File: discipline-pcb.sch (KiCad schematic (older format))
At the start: 164 parts, among them J1 AVR-ISP-6, SW1 KEYSW, SW10 KEYSW, SW11 KEYSW, SW12 KEYSW, SW13 KEYSW, SW14 KEYSW, SW15 KEYSW, SW16 KEYSW, SW17 KEYSW, SW18 KEYSW, SW19 KEYSW, SW2 KEYSW, SW20 KEYSW, SW21 KEYSW, SW22 KEYSW, SW23 KEYSW, SW24 KEYSW, SW25 KEYSW, SW26 KEYSW, SW27 KEYSW, SW28 KEYSW, SW29 KEYSW, SW3 KEYSW, SW30 KEYSW, SW31 KEYSW, SW32 KEYSW, SW33 KEYSW, SW34 KEYSW, SW35 KEYSW, SW36 KEYSW, SW37 KEYSW, SW38 KEYSW, SW39 KEYSW, SW4 KEYSW, SW40 KEYSW, SW41 KEYSW, SW42 KEYSW, SW43 KEYSW, SW44 KEYSW, SW45 KEYSW, SW46 KEYSW, SW47 KEYSW, SW48 KEYSW, SW49 KEYSW, SW5 KEYSW, SW50 KEYSW, SW51 KEYSW, SW52 KEYSW, SW53 KEYSW, SW54 KEYSW, SW55 KEYSW, SW56 KEYSW, SW57 KEYSW, SW58 KEYSW, SW59 KEYSW, SW6 KEYSW, SW60 KEYSW, SW61 KEYSW, SW62 KEYSW, SW63 KEYSW, SW64 KEYSW, SW65 KEYSW, SW66 KEYSW, SW67 KEYSW, SW68 KEYSW, SW69 KEYSW, SW7 KEYSW, SW70 KEYSW, SW71 KEYSW, SW72 KEYSW, SW73 KEYSW, SW74 KEYSW, SW8 KEYSW, SW9 KEYSW, U1 ATmega32A-PU, Y1 Crystal

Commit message: Learning stuff
WIP for an attempt to create an ISO layout + split spacebar + middle
button
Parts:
- removed SW70, SW71, SW73, SW74: KEYSW, cftkb:SW_Cherry_MX1A_1.50u_PCBNOSCREEN, symbol keyboard_parts:KEYSW
- removed SW72: KEYSW, cftkb:SW_Cherry_MX1A_1.00u_PCB-NOSCREEN, symbol keyboard_parts:KEYSW
- added D71, D72: (no value), cftkb:D_DO-35_SOD27_P5.08mm_Horizontal, symbol discipline-pcb-rescue:D-Device
- added SW71: KEYSW, cftkb:SW_Cherry_MX1A_1.00u_PCB-NOSCREEN, symbol discipline-pcb-rescue:KEYSW-keyboard_parts
- added SW72, SW73: KEYSW, cftkb:SW_Cherry_MX1A_3.00u_PCB-NOSCREEN, symbol discipline-pcb-rescue:KEYSW-keyboard_parts
- BOOT1, RESET1: symbol keyboard_parts:SW_PUSH -> discipline-pcb-rescue:SW_PUSH-keyboard_parts
- C1, C2, C4, C5: symbol Device:C_Small -> discipline-pcb-rescue:C_Small-Device
- C3: symbol Device:CP1_Small -> discipline-pcb-rescue:CP1_Small-Device
- D1, D10, D11, D12, D13, D14, D15, D16, D17, D18, D19, D2, D20, D21, D22, D23, D24, D25, D26, D27, D28, D29, D3, D30, D31, D32, D33, D34, D35, D36, D37, D38, D39, D4, D40, D41, D42, D43, D44, D45, D46, D47, D48, D49, D5, D50, D51, D52, D53, D54, D55, D56, D57, D58, D59, D6, D60, D61, D62, D63, D64, D65, D66, D67, D68, D7, D8, D9: symbol Device:D -> discipline-pcb-rescue:D-Device
- D69, D70: symbol Device:D_Zener_Small -> discipline-pcb-rescue:D_Zener_Small-Device
- F1: symbol Device:Polyfuse_Small -> discipline-pcb-rescue:Polyfuse_Small-Device
- J1: symbol Connector:AVR-ISP-6 -> discipline-pcb-rescue:AVR-ISP-6-Connector
- LED1: symbol Device:LED -> discipline-pcb-rescue:LED-Device
- R1, R2, R3, R4, R5, R6, R7: symbol Device:R_Small -> discipline-pcb-rescue:R_Small-Device
- SW1, SW10, SW11, SW12, SW13, SW14, SW15, SW16, SW17, SW18, SW19, SW2, SW20, SW21, SW22, SW23, SW24, SW25, SW26, SW27, SW28, SW29, SW3, SW30, SW31, SW32, SW33, SW34, SW35, SW36, SW37, SW38, SW39, SW4, SW40, SW41, SW42, SW44, SW46, SW47, SW48, SW49, SW5, SW50, SW51, SW52, SW53, SW54, SW55, SW56, SW57, SW58, SW6, SW62, SW65, SW66, SW67, SW68, SW69, SW7, SW8, SW9: symbol keyboard_parts:KEYSW -> discipline-pcb-rescue:KEYSW-keyboard_parts
- SW43: footprint cftkb:SW_Cherry_MX1A_2.25u_PCBNOSCREEN -> cftkb:SW_Cherry_MX1A_1.00u_PCB-NOSCREEN; symbol keyboard_parts:KEYSW -> discipline-pcb-rescue:KEYSW-keyboard_parts
- SW45: footprint cftkb:SW_Cherry_MX1A_2.25u_PCBNOSCREEN -> cftkb:SW_Cherry_MX1A_1.25u_PCBNOSCREEN; symbol keyboard_parts:KEYSW -> discipline-pcb-rescue:KEYSW-keyboard_parts
- SW59, SW60, SW61, SW63, SW64: footprint cftkb:SW_Cherry_MX1A_1.25u_PCBNOSCREEN -> cftkb:SW_Cherry_MX1A_1.00u_PCB-NOSCREEN; symbol keyboard_parts:KEYSW -> discipline-pcb-rescue:KEYSW-keyboard_parts
- U1: symbol MCU_Microchip_ATmega:ATmega32A-PU -> discipline-pcb-rescue:ATmega32A-PU-MCU_Microchip_ATmega
- USB1: symbol Type-C:USB_C_GCT_USB4085 -> discipline-pcb-rescue:USB_C_GCT_USB4085-Type-C
- Y1: symbol Device:Crystal -> discipline-pcb-rescue:Crystal-Device
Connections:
- wire segments 342 -> 340

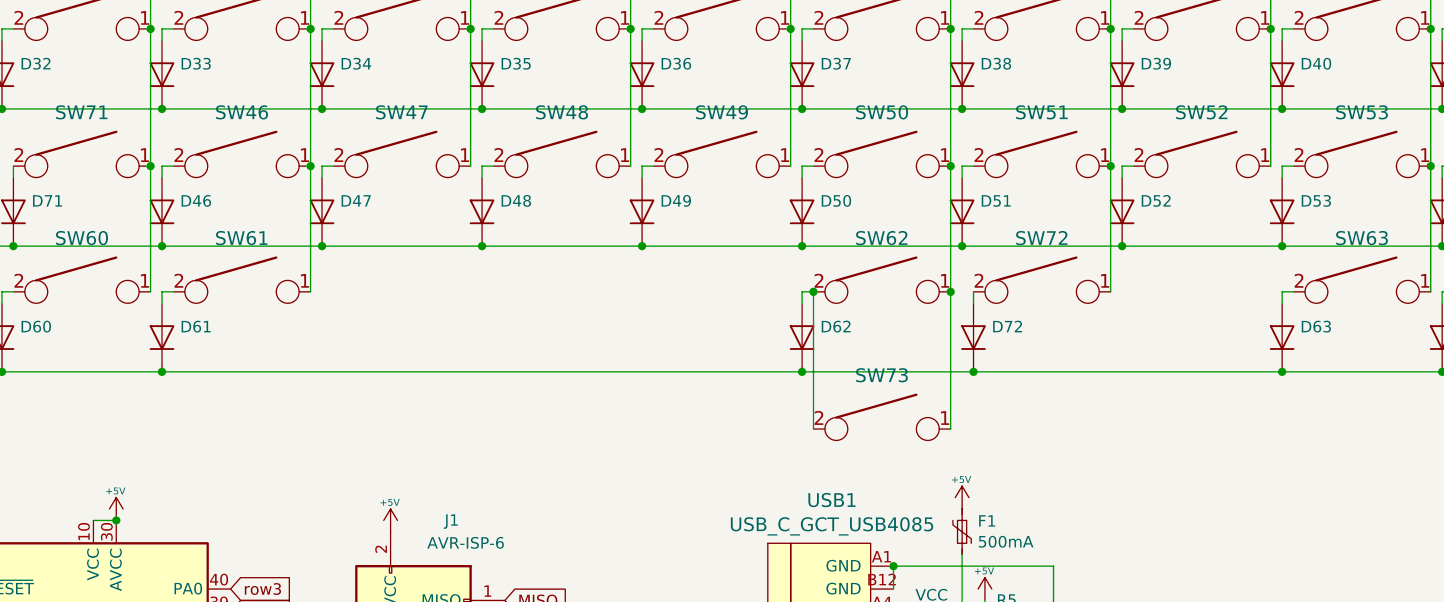
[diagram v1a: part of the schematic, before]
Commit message: Learning stuff
WIP for an attempt to create an ISO layout + split spacebar + middle
button
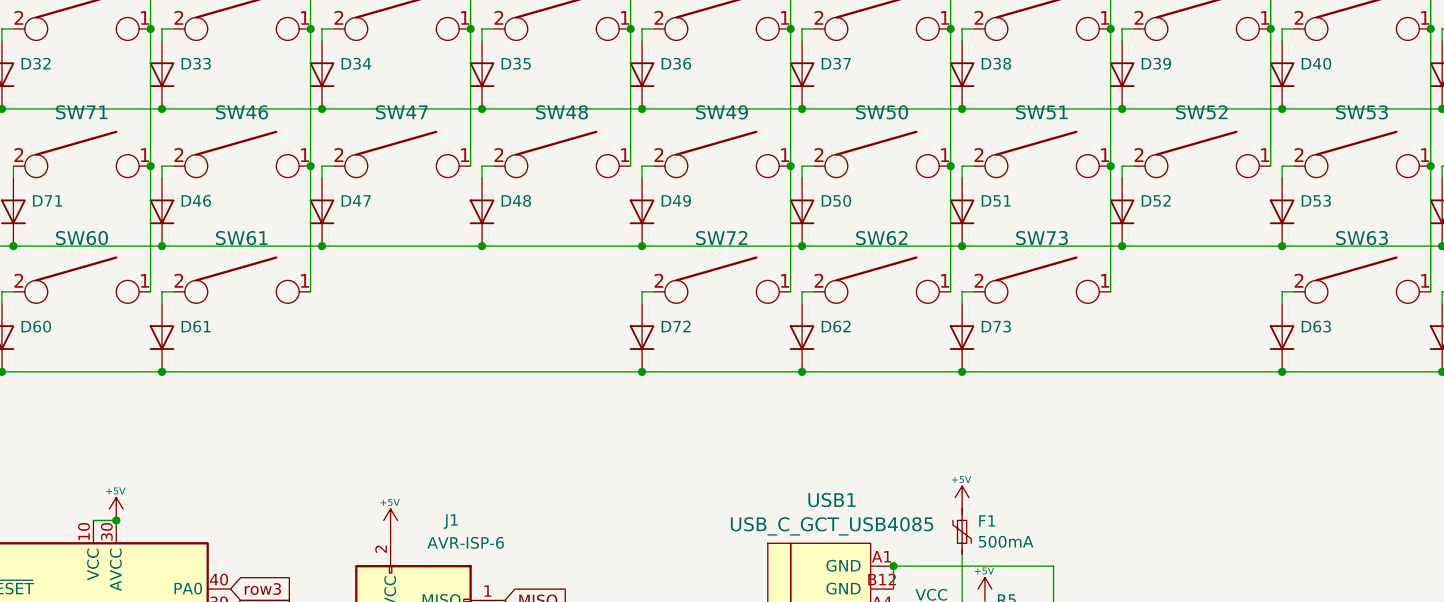
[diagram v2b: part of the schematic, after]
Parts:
- added D73: (no value), cftkb:D_DO-35_SOD27_P5.08mm_Horizontal, symbol discipline-pcb-rescue:D-Device
- C1, C2: footprint cftkb:D_DO-35_SOD27_P5.08mm_Horizontal -> cftkb:C_Disc_D3.0mm_W1.6mm_P2.50mm
- C3: footprint cftkb:D_DO-35_SOD27_P5.08mm_Horizontal -> cftkb:CP_Radial_D4.0mm_P1.50mm
- C4, C5: footprint cftkb:D_DO-35_SOD27_P5.08mm_Horizontal -> cftkb:C_Disc_D4.3mm_W1.9mm_P5.00mm
- SW29: footprint cftkb:SW_Cherry_MX1A_1.50u_PCBNOSCREEN -> cftkb:SW_Cherry_MX1A_ISOEnter_PCB_ReversedStabilizer
- SW72, SW73: footprint cftkb:SW_Cherry_MX1A_3.00u_PCB-NOSCREEN -> cftkb:SW_Cherry_MX1A_3.00u_PCBNOSCREEN
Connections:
- net col5: now also SW72.1
- net col6: no longer SW73.1
- net col7: now also SW73.1; no longer SW72.1
- net row4: now also D73.1 (K)
- net at D62.2 (A), SW62.2: no longer SW73.2
- new net: D73.2 (A), SW73.2
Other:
- moved on the sheet: D72, SW72, SW73
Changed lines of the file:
@@
 F 0 "SW29" H 12350 3733 60  0000 C CNN
 F 1 "KEYSW" H 12350 3400 60  0001 C CNN
-F 2 "cftkb:SW_Cherry_MX1A_1.50u_PCBNOSCREEN" H 12350 3500 60  0001 C CNN
+F 2 "cftkb:SW_Cherry_MX1A_ISOEnter_PCB_ReversedStabilizer" H 12350 3500 60  0001 C CNN
 F 3 "" H 12350 3500 60  0000 C CNN
 	1    12350 3500
@@
 	3600 5600 4300 5600
 Connection ~ 4300 5600
-Wire Wire Line
-	4300 5600 7100 5600
 Wire Wire Line
 	11300 5600 12000 5600
@@
 Wire Wire Line
 	10600 5250 10600 5300
-Connection ~ 7100 5600
 Wire Wire Line
 	9200 5600 9900 5600
@@
 F 0 "C2" H 3100 7300 50  0000 L CNN
 F 1 "22p" H 3100 7200 50  0000 L CNN
-F 2 "cftkb:D_DO-35_SOD27_P5.08mm_Horizontal" H 3000 7200 50  0001 C CNN
+F 2 "cftkb:C_Disc_D3.0mm_W1.6mm_P2.50mm" H 3000 7200 50  0001 C CNN
 F 3 "~" H 3000 7200 50  0001 C CNN
 	1    3000 7200
@@
 F 0 "C1" H 2650 7300 50  0000 L CNN
 F 1 "22p" H 2600 7200 50  0000 L CNN
-F 2 "cftkb:D_DO-35_SOD27_P5.08mm_Horizontal" H 2850 7200 50  0001 C CNN
+F 2 "cftkb:C_Disc_D3.0mm_W1.6mm_P2.50mm" H 2850 7200 50  0001 C CNN
 F 3 "~" H 2850 7200 50  0001 C CNN
 	1    2850 7200
@@
 F 0 "C3" H 5350 10250 50  0000 L CNN
 F 1 "4.7u" H 5300 9950 50  0000 L CNN
-F 2 "cftkb:D_DO-35_SOD27_P5.08mm_Horizontal" H 5400 10100 50  0001 C CNN
+F 2 "cftkb:CP_Radial_D4.0mm_P1.50mm" H 5400 10100 50  0001 C CNN
 F 3 "~" H 5400 10100 50  0001 C CNN
 	1    5400 10100
@@
 F 0 "C4" H 5500 10250 50  0000 L CNN
 F 1 "0.1u" H 5500 9950 50  0000 L CNN
-F 2 "cftkb:D_DO-35_SOD27_P5.08mm_Horizontal" H 5550 10100 50  0001 C CNN
+F 2 "cftkb:C_Disc_D4.3mm_W1.9mm_P5.00mm" H 5550 10100 50  0001 C CNN
 F 3 "~" H 5550 10100 50  0001 C CNN
 	1    5550 10100
@@
 F 0 "C5" H 5650 10250 50  0000 L CNN
 F 1 "0.1u" H 5700 9950 50  0000 L CNN
-F 2 "cftkb:D_DO-35_SOD27_P5.08mm_Horizontal" H 5700 10100 50  0001 C CNN
+F 2 "cftkb:C_Disc_D4.3mm_W1.9mm_P5.00mm" H 5700 10100 50  0001 C CNN
 F 3 "~" H 5700 10100 50  0001 C CNN
 	1    5700 10100
@@
 Wire Wire Line
 	7750 4100 7750 4700
-Connection ~ 7750 4700
-Wire Wire Line
-	7750 4700 7750 5250
 Wire Wire Line
 	8450 2900 8450 2950
@@
 	8450 3500 8450 4100
 Connection ~ 8450 4100
-Wire Wire Line
-	8450 4100 8450 4700
 Wire Wire Line
 	9150 2900 9150 2950
@@
 	1    0    0    -1
 $EndComp
-Connection ~ 8450 4700
-Wire Wire Line
-	8450 4700 8450 5250
+Wire Wire Line
+	7750 4700 7750 5250
 $Comp
 L discipline-pcb-rescue:KEYSW-keyboard_parts SW72
 U 1 1 5EFCCC86
-P 8150 5250
-F 0 "SW72" H 8150 5483 60  0000 C CNN
-F 1 "KEYSW" H 8150 5150 60  0001 C CNN
-F 2 "cftkb:SW_Cherry_MX1A_3.00u_PCB-NOSCREEN" H 8150 5250 60  0001 C CNN
-F 3 "" H 8150 5250 60  0000 C CNN
-	1    8150 5250
+P 6750 5250
+F 0 "SW72" H 6750 5483 60  0000 C CNN
+F 1 "KEYSW" H 6750 5150 60  0001 C CNN
+F 2 "cftkb:SW_Cherry_MX1A_3.00u_PCBNOSCREEN" H 6750 5250 60  0001 C CNN
+F 3 "" H 6750 5250 60  0000 C CNN
+	1    6750 5250
 	1    0    0    -1
 $EndComp
@@
 L discipline-pcb-rescue:D-Device D72
 U 1 1 5EFEEE87
-P 7850 5450
-F 0 "D72" V 7896 5371 50  0000 R CNN
-F 1 " " V 7805 5371 50  0000 R CNN
-F 2 "cftkb:D_DO-35_SOD27_P5.08mm_Horizontal" H 7850 5450 50  0001 C CNN
-F 3 "~" H 7850 5450 50  0001 C CNN
-	1    7850 5450
-	0    -1   -1   0
-$EndComp
-Connection ~ 7850 5600
-Wire Wire Line
-	7850 5600 9200 5600
-Wire Wire Line
-	7850 5250 7850 5300
+P 6400 5450
+F 0 "D72" V 6446 5371 50  0000 R CNN
+F 1 " " V 6355 5371 50  0000 R CNN
+F 2 "cftkb:D_DO-35_SOD27_P5.08mm_Horizontal" H 6400 5450 50  0001 C CNN
+F 3 "~" H 6400 5450 50  0001 C CNN
+	1    6400 5450
+	0    -1   -1   0
+$EndComp
+Wire Wire Line
+	6400 5250 6400 5300
 $Comp
 L discipline-pcb-rescue:KEYSW-keyboard_parts SW71
@@
 L discipline-pcb-rescue:KEYSW-keyboard_parts SW73
 U 1 1 5EFB299D
-P 7450 5850
-F 0 "SW73" H 7450 6083 60  0000 C CNN
-F 1 "KEYSW" H 7450 5750 60  0001 C CNN
-F 2 "cftkb:SW_Cherry_MX1A_3.00u_PCB-NOSCREEN" H 7450 5850 60  0001 C CNN
-F 3 "" H 7450 5850 60  0000 C CNN
-	1    7450 5850
-	1    0    0    -1
-$EndComp
-Wire Wire Line
-	7750 5850 7750 5250
-Connection ~ 7750 5250
-Wire Wire Line
-	7100 5600 7850 5600
-Wire Wire Line
-	7150 5850 7150 5250
-Connection ~ 7150 5250
+P 8150 5250
+F 0 "SW73" H 8150 5483 60  0000 C CNN
+F 1 "KEYSW" H 8150 5150 60  0001 C CNN
+F 2 "cftkb:SW_Cherry_MX1A_3.00u_PCBNOSCREEN" H 8150 5250 60  0001 C CNN
+F 3 "" H 8150 5250 60  0000 C CNN
+	1    8150 5250
+	1    0    0    -1
+$EndComp
+Connection ~ 7750 4700
+Wire Wire Line
+	8450 4100 8450 4700
+Wire Wire Line
+	8450 4700 8450 5250
+Connection ~ 8450 4700
+Wire Wire Line
+	4300 5600 6400 5600
+Connection ~ 7100 5600
+Wire Wire Line
+	7100 5600 7800 5600
+Connection ~ 6400 5600
+Wire Wire Line
+	6400 5600 7100 5600
+$Comp
+L discipline-pcb-rescue:D-Device D73
+U 1 1 5F273FC2
+P 7800 5450
+F 0 "D73" V 7846 5371 50  0000 R CNN
+F 1 " " V 7755 5371 50  0000 R CNN
+F 2 "cftkb:D_DO-35_SOD27_P5.08mm_Horizontal" H 7800 5450 50  0001 C CNN
+F 3 "~" H 7800 5450 50  0001 C CNN
+	1    7800 5450
+	0    -1   -1   0
+$EndComp
+Wire Wire Line
+	6450 5250 6400 5250
+Connection ~ 7800 5600
+Wire Wire Line
+	7800 5600 9200 5600
+Wire Wire Line
+	7850 5250 7800 5250
+Wire Wire Line
+	7800 5250 7800 5300
+Wire Wire Line
+	7050 4700 7050 5250
+Connection ~ 7050 4700
 $EndSCHEMATC

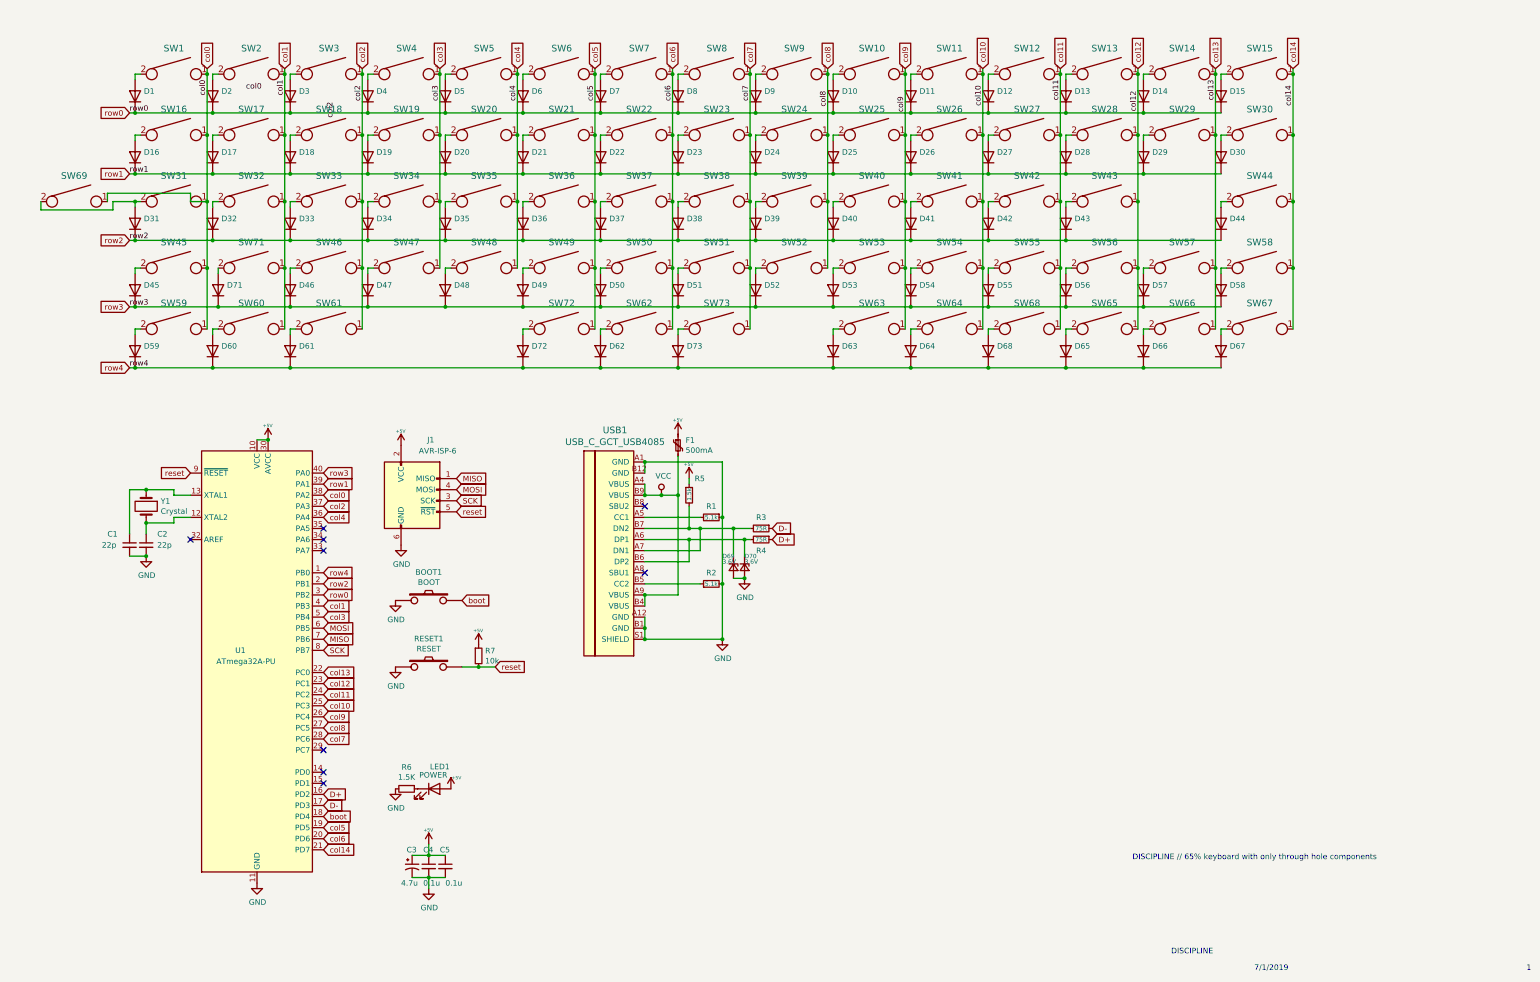
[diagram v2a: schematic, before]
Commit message: "Split spacebar + middle button" design completed
Re-integrated ANSI/ISO layout from coseyfannitutti v2, made some
corrections, added logo...
PCB proto is ordered, let's see how it turns out.
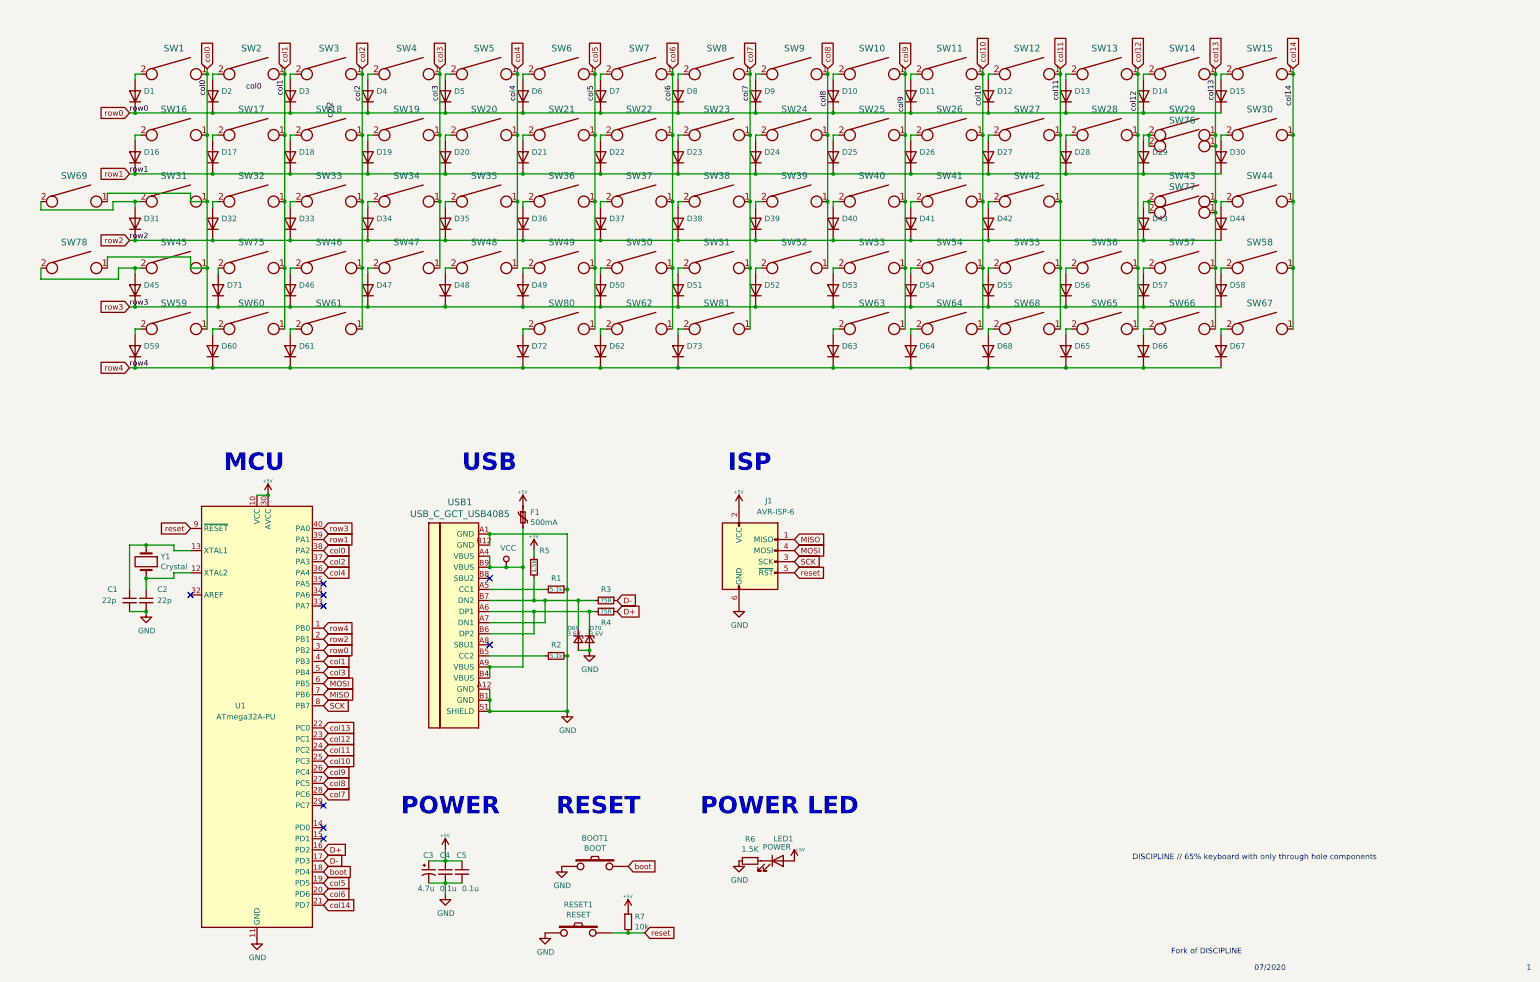
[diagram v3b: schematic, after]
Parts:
- added SW76: KEYSW, cftkb:SW_Cherry_MX1A_ISOEnter_PCB_ReversedStabilizer, symbol discipline-pcb-rescue:KEYSW-keyboard_parts
- added SW77: KEYSW, cftkb:SW_Cherry_MX1A_1.00u_PCB-NOSCREEN, symbol discipline-pcb-rescue:KEYSW-keyboard_parts
- added SW78: KEYSW, cftkb:SW_Cherry_MX1A_1.25u_PCBNOSCREEN, symbol discipline-pcb-rescue:KEYSW-keyboard_parts
- SW29: footprint cftkb:SW_Cherry_MX1A_ISOEnter_PCB_ReversedStabilizer -> cftkb:SW_Cherry_MX1A_1.50u_PCBNOSCREEN
- SW43: footprint cftkb:SW_Cherry_MX1A_1.00u_PCB-NOSCREEN -> cftkb:SW_Cherry_MX1A_2.25u_PCBNOSCREEN
- SW63: footprint cftkb:SW_Cherry_MX1A_1.00u_PCB-NOSCREEN -> cftkb:SW_Cherry_MX1A_1.25u_PCBNOSCREEN
- renumbered SW71 to SW75, SW72 to SW80, SW73 to SW81
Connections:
- net col0: now also SW78.1
- net col12: no longer SW43.1
- net col13: now also SW43.1, SW76.1, SW77.1
- net at D29.2 (A), SW29.2: now also SW76.2
- net at D43.2 (A), SW43.2: now also SW77.2
- net at D45.2 (A), SW45.2: now also SW78.2
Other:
- note added: "07/2020"
- note added: "Fork of DISCIPLINE"
- note added: "ISP"
- note added: "MCU"
- note added: "POWER"
- note added: "POWER LED"
- note added: "RESET"
- note added: "USB"
- note removed: "7/1/2019"
- note removed: "DISCIPLINE"
- moved on the sheet: BOOT1, C1, C2, C3, C4, C5, D43, D69, D70, F1, J1, LED1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
